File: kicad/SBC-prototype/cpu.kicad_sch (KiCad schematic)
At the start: 1 part, among them IC2 W65C02S6TPG-14

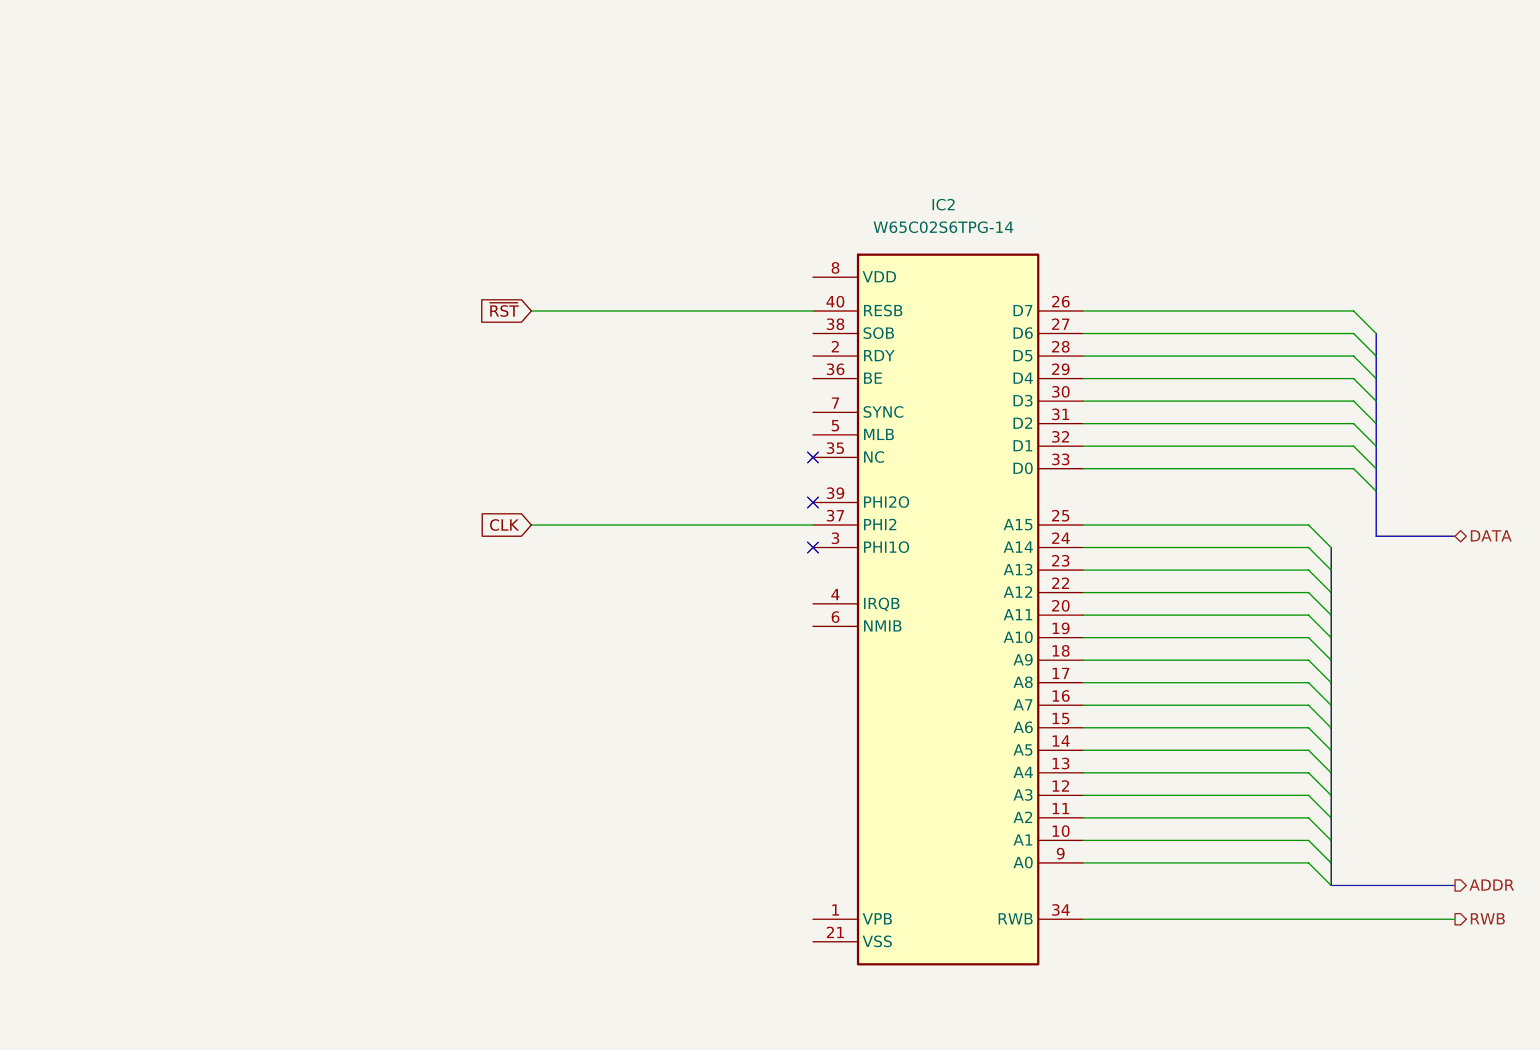
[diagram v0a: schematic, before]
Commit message: Adding SRAM and EEPROM to schematic
- Also ignoring all Kicad backup .zip files
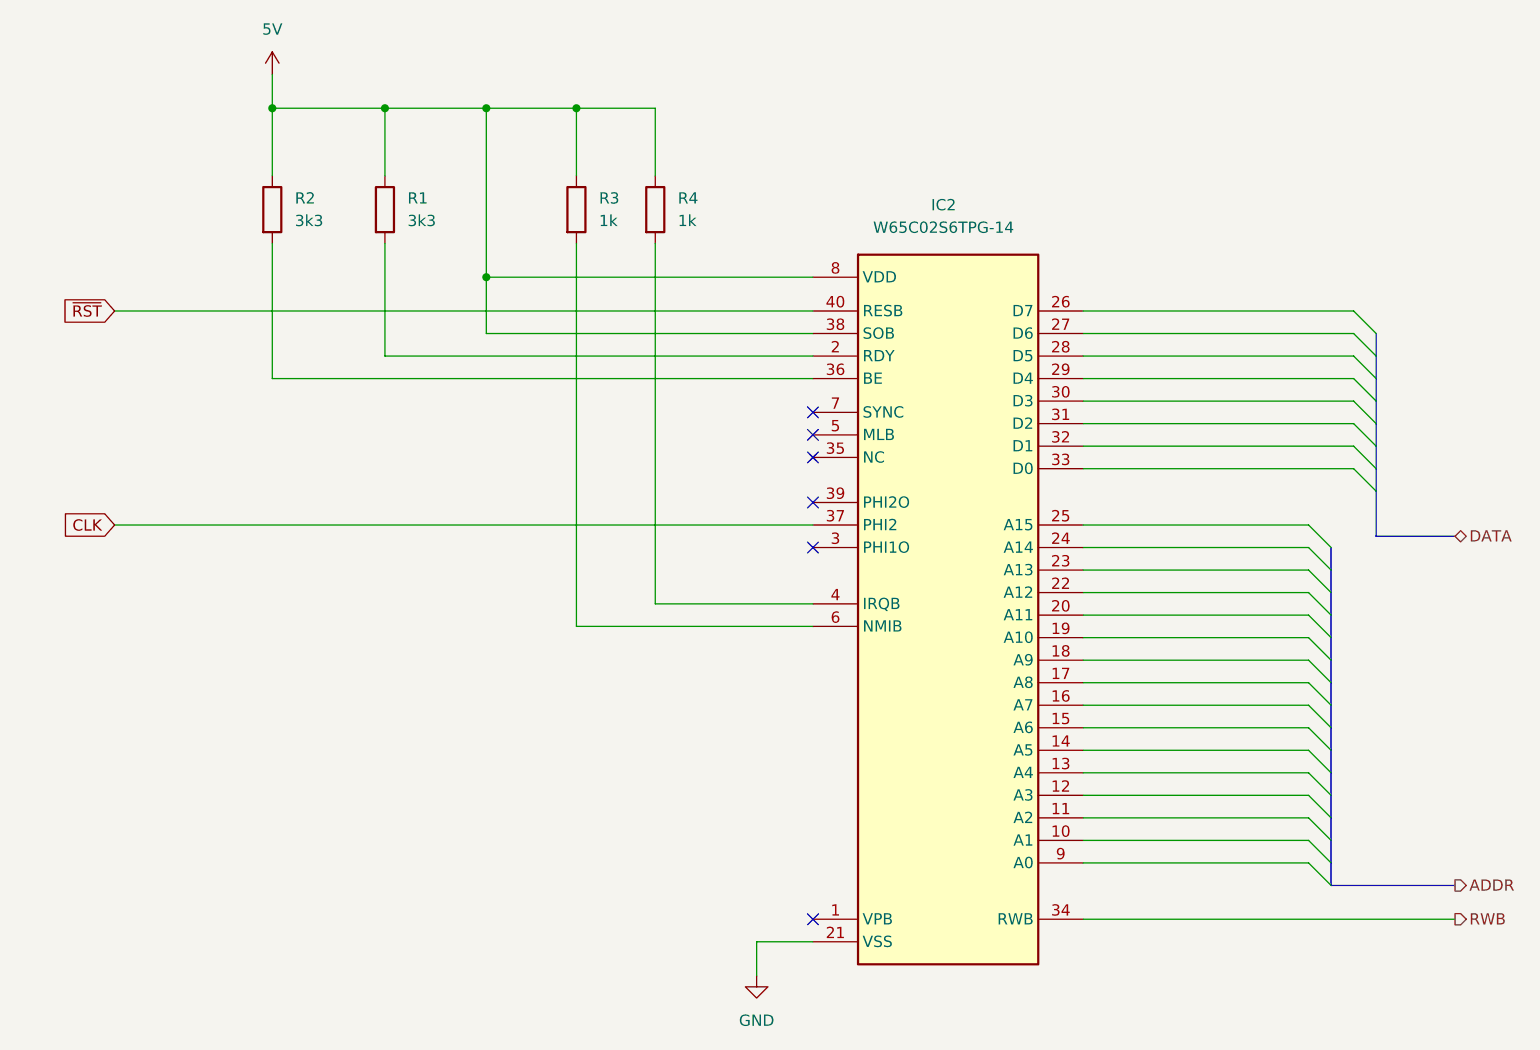
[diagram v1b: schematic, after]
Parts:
- added R1, R2: 3k3, symbol Device:R
- added R3, R4: 1k, symbol Device:R
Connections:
- net at IC2.2 (RDY): now also R1.2
- net GND: now reaches IC2.21 (VSS)
- net at IC2.36 (BE): now also R2.2
- net 5V: now reaches IC2.38 (SOB)
- net 5V: now also IC2.8 (VDD), R1.1, R2.1, R3.1, R4.1
- net at IC2.4 (IRQB): now also R4.2
- net at IC2.6 (NMIB): now also R3.2
- no-connect marks 3 -> 6
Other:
- title: (none) -> 65C02 Single Board Computer
